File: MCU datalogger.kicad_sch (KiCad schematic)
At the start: 25 parts, among them U1 24LC1025, U2 24LC1025, U3 DS1337S_, U4 ATMEGA328P-AU, Y1 Crystal, Y2 Crystal

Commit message: completed symbols footprints association
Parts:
- BT1: footprint (none) -> Connector_PinHeader_2.54mm:PinHeader_1x02_P2.54mm_Vertical
- C1, C4: value C -> 0.1uF; footprint (none) -> Capacitor_SMD:C_0805_2012Metric
- C2: renamed from C3; value C -> 22pF; footprint (none) -> Capacitor_SMD:C_0805_2012Metric
- C3: renamed from C2; value C -> 22pF; footprint (none) -> Capacitor_SMD:C_0805_2012Metric
- C5: value C_Polarized -> 100nF; footprint (none) -> Capacitor_SMD:C_0805_2012Metric
- D1, D2: footprint (none) -> LED_SMD:LED_0805_2012Metric
- H1, H2, H3, H4: footprint (none) -> MountingHole:MountingHole_2.1mm
- R1: renamed from R3; value R -> 10K; footprint (none) -> Resistor_SMD:R_0805_2012Metric
- R2: renamed from R4; value R -> 10K; footprint (none) -> Resistor_SMD:R_0805_2012Metric
- R3: renamed from R1; value R -> 4.7K; footprint (none) -> Resistor_SMD:R_0805_2012Metric
- R4: renamed from R2; value R -> 4.7K; footprint (none) -> Resistor_SMD:R_0805_2012Metric
- R5, R7: value R -> 330; footprint (none) -> Resistor_SMD:R_0805_2012Metric
- R6: value R -> 10K; footprint (none) -> Resistor_SMD:R_0805_2012Metric
- U1, U2: footprint (none) -> Package_SO:SOIC-8_5.3x5.3mm_P1.27mm
- U3: footprint DS1337S_:SOIC127P600X175-8N -> footprints:SOIC127P600X175-8N
- U4: footprint ATMEGA328P-AU:QFP80P900X900X120-32N -> footprints:QFP80P900X900X120-32N
- Y1: value Crystal -> 16 MHz; footprint (none) -> Crystal:Crystal_SMD_5032-2Pin_5.0x3.2mm_HandSoldering
- Y2: value Crystal -> 32.768 KHz; footprint (none) -> Crystal:Crystal_SMD_5032-2Pin_5.0x3.2mm_HandSoldering
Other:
- moved on the sheet: R2, R4
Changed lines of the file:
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@@
 			)
 		)
-		(property "Value" "R"
+		(property "Value" "330"
 			(at 157.48 60.96 90)
 			(effects
@@
 			)
 		)
-		(property "Footprint" ""
+		(property "Footprint" "Resistor_SMD:R_0805_2012Metric"
 			(at 157.48 66.548 90)
 			(effects
@@
 			)
 		)
-		(property "Footprint" "DS1337S_:SOIC127P600X175-8N"
+		(property "Footprint" "footprints:SOIC127P600X175-8N"
 			(at 71.12 81.28 0)
 			(effects
@@
 			)
 		)
-		(property "Footprint" ""
+		(property "Footprint" "LED_SMD:LED_0805_2012Metric"
 			(at 231.14 80.01 0)
 			(effects
@@
 		(dnp no)
 		(fields_autoplaced yes)
-		(property "Reference" "R3"
+		(property "Reference" "R1"
 			(at 102.87 69.8499 0)
 			(effects
@@
 			)
 		)
-		(property "Value" "R"
+		(property "Value" "10K"
 			(at 102.87 72.3899 0)
 			(effects
@@
 			)
 		)
-		(property "Footprint" ""
+		(property "Footprint" "Resistor_SMD:R_0805_2012Metric"
 			(at 98.552 71.12 90)
 			(effects
@@
 			(project ""
 				(path "/0f894c6c-65ea-4f50-8650-194ad04aa300"
-					(reference "R3")
+					(reference "R1")
 					(unit 1)
 				)
@@
 			)
 		)
-		(property "Footprint" ""
+		(property "Footprint" "MountingHole:MountingHole_2.1mm"
 			(at 223.52 144.78 0)
 			(effects
@@
 			)
 		)
-		(property "Footprint" ""
+		(property "Footprint" "LED_SMD:LED_0805_2012Metric"
 			(at 177.8 64.77 0)
 			(effects
@@
 			)
 		)
-		(property "Value" "C_Polarized"
+		(property "Value" "100nF"
 			(at 241.3 67.6909 0)
 			(effects
@@
 			)
 		)
-		(property "Footprint" ""
+		(property "Footprint" "Capacitor_SMD:C_0805_2012Metric"
 			(at 238.4552 71.12 0)
 			(effects
@@
 		(dnp no)
 		(fields_autoplaced yes)
-		(property "Reference" "C2"
+		(property "Reference" "C3"
 			(at 161.29 88.8999 0)
 			(effects
@@
 			)
 		)
-		(property "Value" "C"
+		(property "Value" "22pF"
 			(at 161.29 91.4399 0)
 			(effects
@@
 			)
 		)
-		(property "Footprint" ""
+		(property "Footprint" "Capacitor_SMD:C_0805_2012Metric"
 			(at 158.4452 93.98 0)
 			(effects
@@
 			(project ""
 				(path "/0f894c6c-65ea-4f50-8650-194ad04aa300"
-					(reference "C2")
+					(reference "C3")
 					(unit 1)
 				)
@@
 			)
 		)
-		(property "Value" "C"
+		(property "Value" "0.1uF"
 			(at 124.46 72.3899 0)
 			(effects
@@
 			)
 		)
-		(property "Footprint" ""
+		(property "Footprint" "Capacitor_SMD:C_0805_2012Metric"
 			(at 121.6152 74.93 0)
 			(effects
@@
 	(symbol
 		(lib_id "Device:R")
-		(at 125.73 132.08 0)
+		(at 127 132.08 0)
 		(unit 1)
 		(exclude_from_sim no)
@@
 		(dnp no)
 		(fields_autoplaced yes)
-		(property "Reference" "R2"
-			(at 128.27 130.8099 0)
-			(effects
-				(font
-					(size 1.27 1.27)
-				)
-				(justify left)
-			)
-		)
-		(property "Value" "R"
-			(at 128.27 133.3499 0)
-			(effects
-				(font
-					(size 1.27 1.27)
-				)
-				(justify left)
-			)
-		)
-		(property "Footprint" ""
-			(at 123.952 132.08 90)
+		(property "Reference" "R4"
+			(at 129.54 130.8099 0)
+			(effects
+				(font
+					(size 1.27 1.27)
+				)
+				(justify left)
+			)
+		)
+		(property "Value" "4.7K"
+			(at 129.54 133.3499 0)
+			(effects
+				(font
+					(size 1.27 1.27)
+				)
+				(justify left)
+			)
+		)
+		(property "Footprint" "Resistor_SMD:R_0805_2012Metric"
+			(at 125.222 132.08 90)
 			(effects
 				(font
@@
 		)
 		(property "Datasheet" "~"
-			(at 125.73 132.08 0)
+			(at 127 132.08 0)
 			(effects
 				(font
@@
 		)
 		(property "Description" "Resistor"
-			(at 125.73 132.08 0)
+			(at 127 132.08 0)
 			(effects
 				(font
@@
 			(project ""
 				(path "/0f894c6c-65ea-4f50-8650-194ad04aa300"
-					(reference "R2")
+					(reference "R4")
 					(unit 1)
 				)
@@
 		(dnp no)
 		(fields_autoplaced yes)
-		(property "Reference" "C3"
+		(property "Reference" "C2"
 			(at 161.29 76.1999 0)
 			(effects
@@
 			)
 		)
-		(property "Value" "C"
+		(property "Value" "22pF"
 			(at 161.29 78.7399 0)
 			(effects
@@
 			)
 		)
-		(property "Footprint" ""
+		(property "Footprint" "Capacitor_SMD:C_0805_2012Metric"
 			(at 158.4452 81.28 0)
 			(effects
@@
 			(project ""
 				(path "/0f894c6c-65ea-4f50-8650-194ad04aa300"
-					(reference "C3")
+					(reference "C2")
 					(unit 1)
 				)
@@
 			)
 		)
-		(property "Footprint" "ATMEGA328P-AU:QFP80P900X900X120-32N"
+		(property "Footprint" "footprints:QFP80P900X900X120-32N"
 			(at 203.2 81.28 0)
 			(effects
@@
 			)
 		)
-		(property "Footprint" ""
+		(property "Footprint" "MountingHole:MountingHole_2.1mm"
 			(at 223.52 153.67 0)
 			(effects
@@
 			)
 		)
-		(property "Value" "R"
+		(property "Value" "10K"
 			(at 176.53 96.52 90)
 			(effects
@@
 			)
 		)
-		(property "Footprint" ""
+		(property "Footprint" "Resistor_SMD:R_0805_2012Metric"
 			(at 176.53 102.108 90)
 			(effects
@@
 			)
 		)
-		(property "Value" "Crystal"
+		(property "Value" "16 MHz"
 			(at 180.34 85.0899 90)
 			(effects
@@
 			)
 		)
-		(property "Footprint" ""
+		(property "Footprint" "Crystal:Crystal_SMD_5032-2Pin_5.0x3.2mm_HandSoldering"
 			(at 176.53 83.82 0)
 			(effects
@@
 			)
 		)
-		(property "Footprint" ""
+		(property "Footprint" "Package_SO:SOIC-8_5.3x5.3mm_P1.27mm"
 			(at 97.79 132.08 0)
 			(effects
@@
 			)
 		)
-		(property "Footprint" ""
+		(property "Footprint" "MountingHole:MountingHole_2.1mm"
 			(at 223.52 134.62 0)
 			(effects
@@
 			)
 		)
-		(property "Value" "Crystal"
+		(property "Value" "32.768 KHz"
 			(at 41.91 83.8199 90)
 			(effects
@@
 			)
 		)
-		(property "Footprint" ""
+		(property "Footprint" "Crystal:Crystal_SMD_5032-2Pin_5.0x3.2mm_HandSoldering"
 			(at 38.1 82.55 0)
 			(effects
@@
 		(dnp no)
 		(fields_autoplaced yes)
-		(property "Reference" "R1"
+		(property "Reference" "R3"
 			(at 120.65 130.8099 0)
 			(effects
@@
 			)
 		)
-		(property "Value" "R"
+		(property "Value" "4.7K"
 			(at 120.65 133.3499 0)
 			(effects
@@
 			)
 		)
-		(property "Footprint" ""
+		(property "Footprint" "Resistor_SMD:R_0805_2012Metric"
 			(at 116.332 132.08 90)
 			(effects
@@
 			(project ""
 				(path "/0f894c6c-65ea-4f50-8650-194ad04aa300"
-					(reference "R1")
+					(reference "R3")
 					(unit 1)
 				)
@@
 			)
 		)
-		(property "Value" "R"
+		(property "Value" "330"
 			(at 233.68 95.2499 0)
 			(effects
@@
 			)
 		)
-		(property "Footprint" ""
+		(property "Footprint" "Resistor_SMD:R_0805_2012Metric"
 			(at 229.362 93.98 90)
 			(effects
@@
 			)
 		)
-		(property "Value" "C"
+		(property "Value" "0.1uF"
 			(at 176.53 46.99 90)
 			(effects
@@
 			)
 		)
-		(property "Footprint" ""
+		(property "Footprint" "Capacitor_SMD:C_0805_2012Metric"
 			(at 180.34 51.1048 0)
 			(effects
@@
 	(symbol
 		(lib_id "Device:R")
-		(at 107.95 71.12 0)
+		(at 109.22 71.12 0)
 		(unit 1)
 		(exclude_from_sim no)
@@
 		(dnp no)
 		(fields_autoplaced yes)
-		(property "Reference" "R4"
-			(at 110.49 69.8499 0)
-			(effects
-				(font
-					(size 1.27 1.27)
-				)
-				(justify left)
-			)
-		)
-		(property "Value" "R"
-			(at 110.49 72.3899 0)
-			(effects
-				(font
-					(size 1.27 1.27)
-				)
-				(justify left)
-			)
-		)
-		(property "Footprint" ""
-			(at 106.172 71.12 90)
+		(property "Reference" "R2"
+			(at 111.76 69.8499 0)
+			(effects
+				(font
+					(size 1.27 1.27)
+				)
+				(justify left)
+			)
+		)
+		(property "Value" "10K"
+			(at 111.76 72.3899 0)
+			(effects
+				(font
+					(size 1.27 1.27)
+				)
+				(justify left)
+			)
+		)
+		(property "Footprint" "Resistor_SMD:R_0805_2012Metric"
+			(at 107.442 71.12 90)
 			(effects
 				(font
@@
 		)
 		(property "Datasheet" "~"
-			(at 107.95 71.12 0)
+			(at 109.22 71.12 0)
 			(effects
 				(font
@@
 		)
 		(property "Description" "Resistor"
-			(at 107.95 71.12 0)
+			(at 109.22 71.12 0)
 			(effects
 				(font
@@
 			(project ""
 				(path "/0f894c6c-65ea-4f50-8650-194ad04aa300"
-					(reference "R4")
+					(reference "R2")
 					(unit 1)
 				)
@@
 			)
 		)
-		(property "Footprint" ""
+		(property "Footprint" "Package_SO:SOIC-8_5.3x5.3mm_P1.27mm"
 			(at 66.04 132.08 0)
 			(effects
@@
 			)
 		)
-		(property "Footprint" ""
+		(property "Footprint" "MountingHole:MountingHole_2.1mm"
 			(at 223.52 125.73 0)
 			(effects
@@
 			)
 		)
-		(property "Footprint" ""
+		(property "Footprint" "Connector_PinHeader_2.54mm:PinHeader_1x02_P2.54mm_Vertical"
 			(at 250.19 65.786 90)
 			(effects

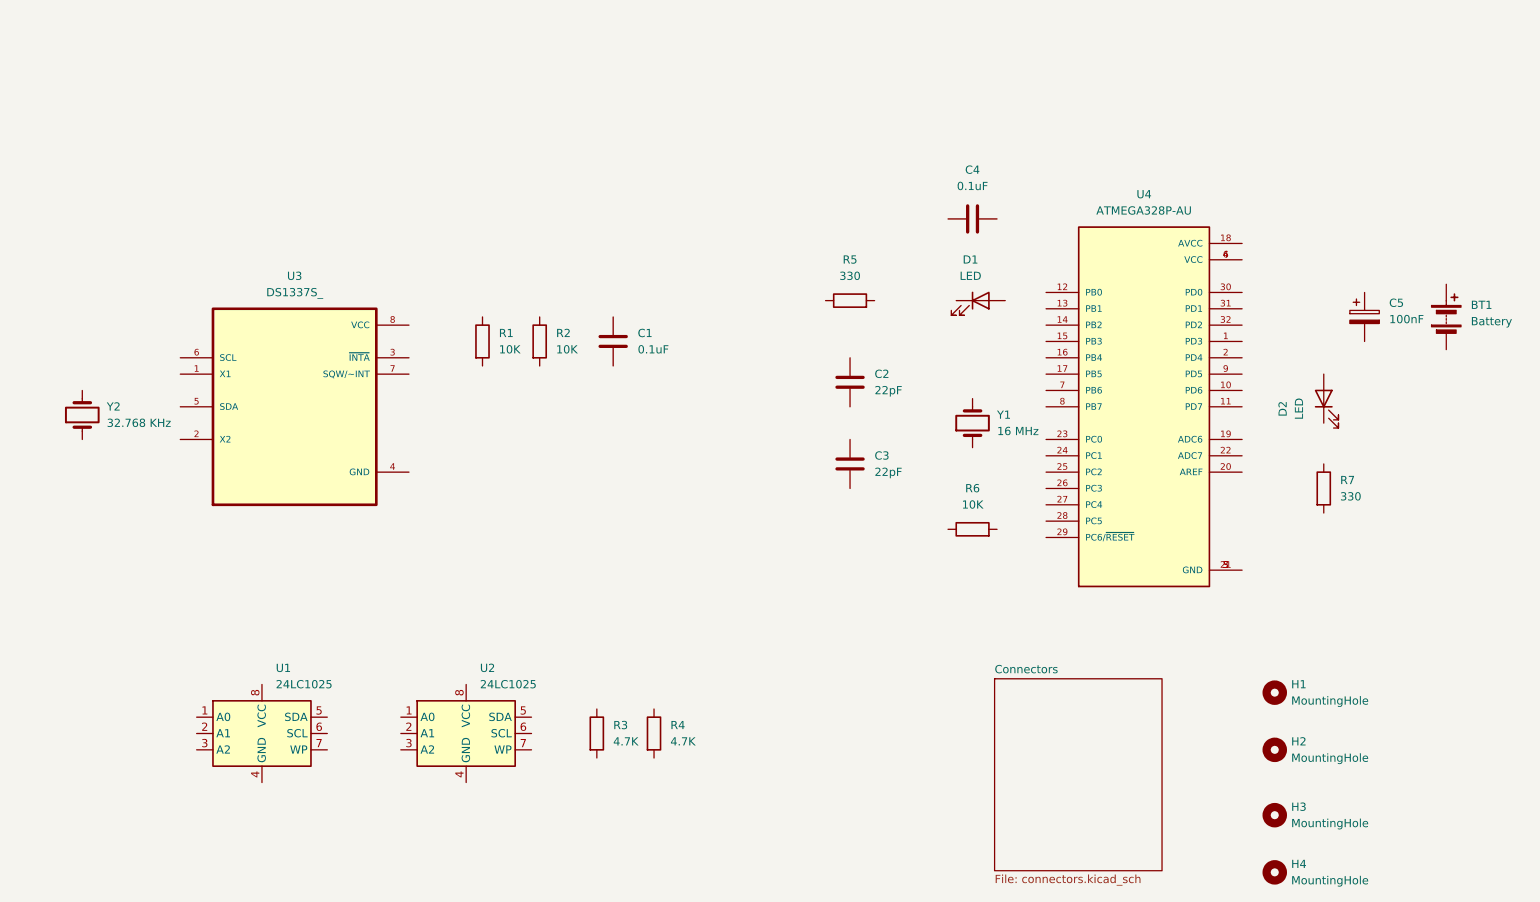
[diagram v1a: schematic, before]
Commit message: Completed wiring of main sheet
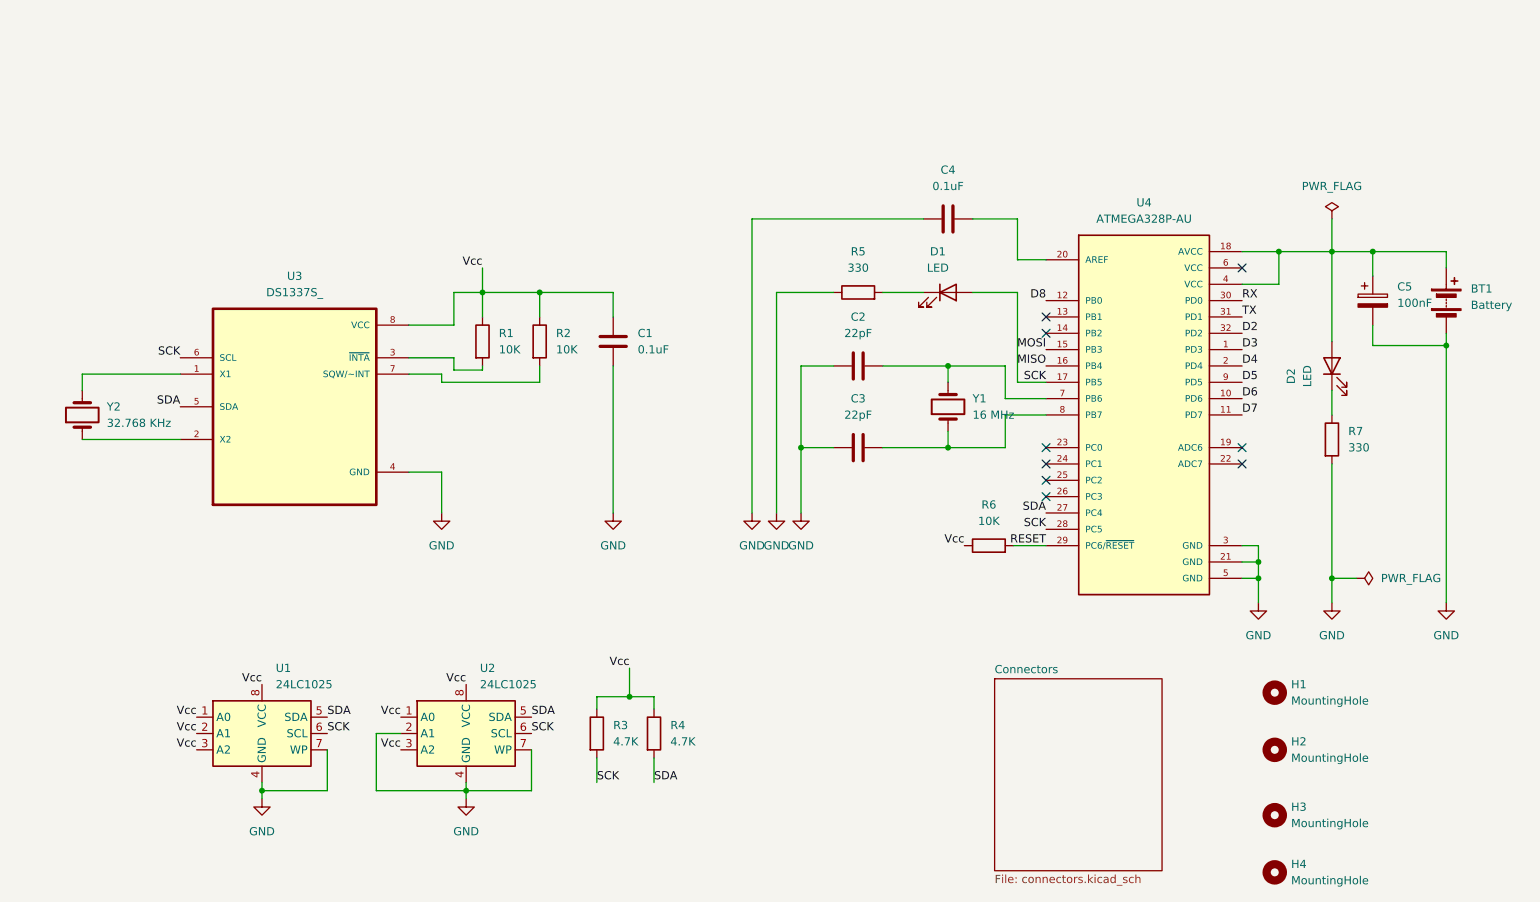
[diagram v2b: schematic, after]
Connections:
- net GND: now reaches R5.1
- net GND: now also BT1.2 (-), C1.2, C2.1, C3.1, C4.1, C5.2, R7.2, U1.4 (GND), U1.7 (WP), U2.2 (A1), U2.4 (GND), U2.7 (WP), U3.4 (GND), U4.21 (GND), U4.3 (GND), U4.5 (GND)
- net at R5.2: now also D1.1 (K)
- net at U3.1 (X1): now also Y2.2
- net at U3.2 (X2): now also Y2.1
- net at U3.3 (~{INTA}): now also R1.2
- net SDA: now reaches U3.5 (SDA)
- net SDA: now also R4.2, U1.5 (SDA), U2.5 (SDA), U4.27 (PC4)
- net SCK: now reaches U3.6 (SCL)
- net SCK: now also D1.2 (A), R3.2, U1.6 (SCL), U2.6 (SCL), U4.17 (PB5), U4.28 (PC5)
- net at U3.7 (SQW/~INT): now also R2.2
- net Vcc: now reaches U3.8 (VCC)
- net Vcc: now also C1.1, R1.1, R2.1, R3.1, R4.1, R6.1, U1.1 (A0), U1.2 (A1), U1.3 (A2), U1.8 (VCC), U2.1 (A0), U2.3 (A2), U2.8 (VCC)
- net at D2.1 (K): now also R7.1
- net at D2.2 (A): now also BT1.1 (+), C5.1, U4.18 (AVCC), U4.4 (VCC)
- net at C3.2: now also U4.8 (PB7), Y1.1
- net at C2.2: now also U4.7 (PB6), Y1.2
- net D3: now reaches U4.1 (PD3)
- net D6: now reaches U4.10 (PD6)
- net D7: now reaches U4.11 (PD7)
- net D8: now reaches U4.12 (PB0)
- net MOSI: now reaches U4.15 (PB3)
- net MISO: now reaches U4.16 (PB4)
- net D4: now reaches U4.2 (PD4)
- net at U4.20 (AREF): now also C4.2
- net RESET: now reaches U4.29 (PC6/~{RESET})
- net RESET: now also R6.2
- net RX: now reaches U4.30 (PD0)
- net TX: now reaches U4.31 (PD1)
- net D2: now reaches U4.32 (PD2)
- net at U4.6 (VCC): no longer U4.4 (VCC)
- net D5: now reaches U4.9 (PD5)
- no-connect marks 0 -> 9
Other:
- moved on the sheet: BT1, C2, C3, C4, C5, D1, D2, R5, R6, R7, Y1

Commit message: changes in both sheets
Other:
- sheet Connectors ports: added D2, D3, D4, D5, D6, D7, D8, GND, MISO, MOSI, RESET, RX, SCK, SDA, TX, Vcc; removed none
- moved on the sheet: BT1, C1, C2, C3, C4, C5, D1, D2, R1, R2, R3, R4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

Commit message: Completed Schematic dsgn
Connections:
- net Vcc: now also R1.2; no longer R1.1
- net at U3.3 (~{INTA}): now also R1.1; no longer R1.2
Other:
- note added: "EEPROM"
- note added: "MCU"
- note added: "Mounting"
- note added: "Real Time Clock"
- moved on the sheet: R1, R2

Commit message: Completed Design of 2-layer
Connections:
- net Vcc: now also BT1.1 (+), C5.1, D2.2 (A), U4.18 (AVCC), U4.4 (VCC)
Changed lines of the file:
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@@
+	)
+	(label "Vcc"
+		(at 240.03 40.64 0)
+		(effects
+			(font
+				(size 1.27 1.27)
+			)
+			(justify left bottom)
+		)
 	)
 	(label "Vcc"
@@
 			)
 			(justify right bottom)
-		)
-	)
-	(rule_area
-		(polyline
-			(pts
-				(xy 27.94 31.75) (xy 127 31.75) (xy 127 90.17) (xy 27.94 90.17)
-			)
-			(stroke
-				(width 0)
-				(type dash)
-				(color 0 0 255 1)
-			)
-			(fill
-				(type color)
-				(color 255 255 255 1)
-			)
-		)
-	)
-	(rule_area
-		(polyline
-			(pts
-				(xy 30.48 105.41) (xy 115.57 105.41) (xy 115.57 138.43) (xy 30.48 138.43)
-			)
-			(stroke
-				(width 0)
-				(type dash)
-				(color 0 0 255 1)
-			)
-			(fill
-				(type color)
-				(color 255 255 255 1)
-			)
 		)
 	)
@@
 			)
 			(stroke
+				(width 0)
+				(type dash)
+				(color 0 0 255 1)
+			)
+			(fill
+				(type color)
+				(color 255 255 255 1)
+			)
+		)
+	)
+	(rule_area
+		(polyline
+			(pts
+				(xy 30.48 105.41) (xy 115.57 105.41) (xy 115.57 138.43) (xy 30.48 138.43)
+			)
+			(stroke
+				(width 0)
+				(type dash)
+				(color 0 0 255 1)
+			)
+			(fill
+				(type color)
+				(color 255 255 255 1)
+			)
+		)
+	)
+	(rule_area
+		(polyline
+			(pts
+				(xy 27.94 31.75) (xy 127 31.75) (xy 127 90.17) (xy 27.94 90.17)
+			)
+			(stroke
